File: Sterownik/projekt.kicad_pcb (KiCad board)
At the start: 2 copper layers, 59.7 x 52.1 mm, 73 parts, among them P3 CONN_01X05, P4 CONN_01X02, P5 CONN_01X02, P6 USB_OTG, P7 CONN_01X12, P8 CONN_01X02, SW1 SW_PUSH_SMALL, T1 Si2323DS, T10 Si2323DS, T12 2N7002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

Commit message: Additional changes
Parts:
- moved R14 7.85 mm to (193.5, 105.5), turned to 270 degrees
- moved R13 2.93 mm to (191.8, 105.5), turned to 90 degrees
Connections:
- C20 pad 1: VUSB_BUS -> VBUS
- C39 pad 1: VUSB_BUS -> VBUS
- C40 pad 1: VUSB_BUS -> VBUS
- C41 pad 1: VUSB_BUS -> VBUS
- R5 pad 1: VUSB_BUS -> VBUS
- T1 pad S: VUSB_BUS -> VBUS
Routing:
- net ON_BUT: track 7.24 -> 98.0 mm, vias 0 -> 1
- net CHARGE_SIGNAL: track 11.8 -> 51.0 mm, vias 0 -> 2
- net VUSB_BUS: track 14.7 -> 48.0 mm
- net MAIN_VOL: track 23.3 -> 44.2 mm, vias 2 -> 3
- net VON: track 20.0 -> 38.6 mm
- net CHARGE_ENABLE: track 20.0 -> 32.2 mm, vias 2 -> 4
- net TERMINATE: track 7.56 -> 15.1 mm
- net VBAT_ADC: track 18.2 -> 23.1 mm
- net VBUS: track 39.1 -> 42.5 mm
- net VBATTERY: track 19.8 -> 18.3 mm
- net MAINTAIN: track 45.2 -> 46.6 mm
- net Net-(R2-Pad1): track 12.8 -> 11.8 mm
- net GND: track 285.6 -> 286.3 mm
- net (no net): track 0.00 -> 0.51 mm

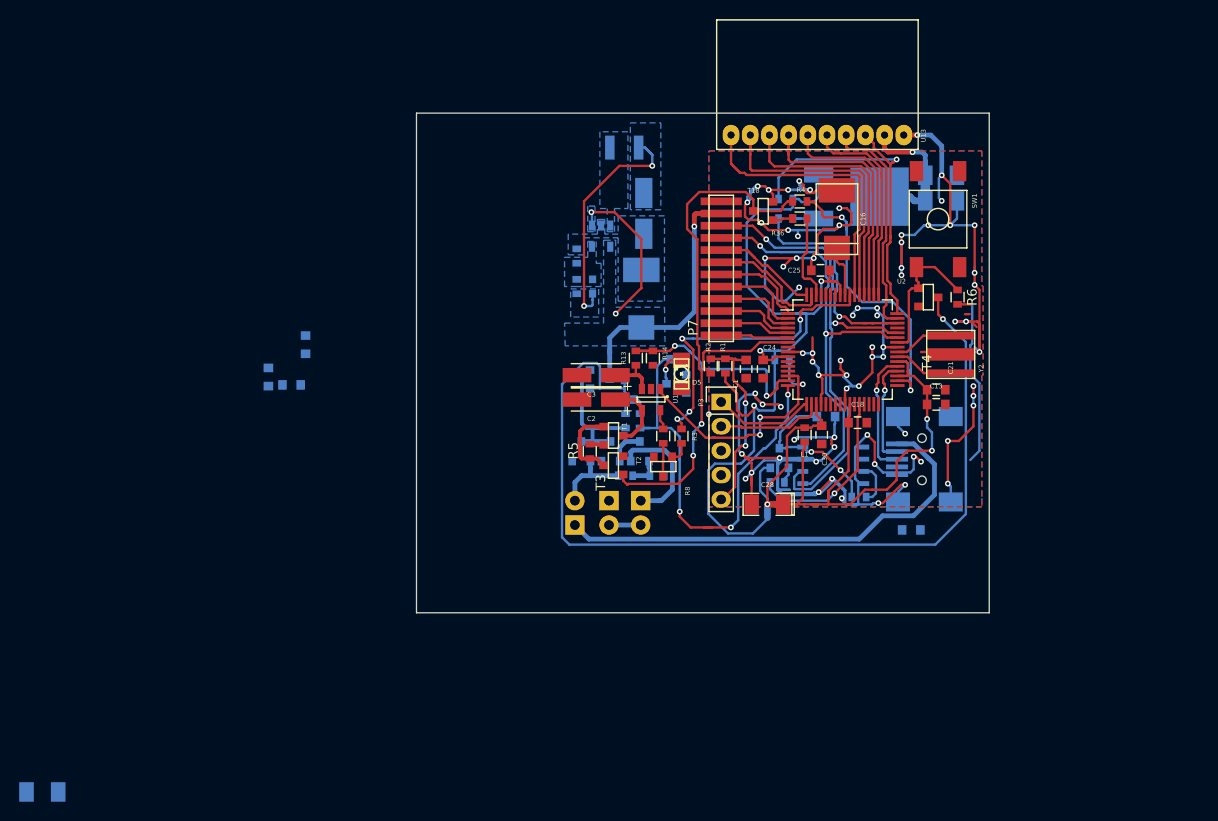
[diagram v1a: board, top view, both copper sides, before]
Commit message: 100% driver PCB routed - waiting for fixes
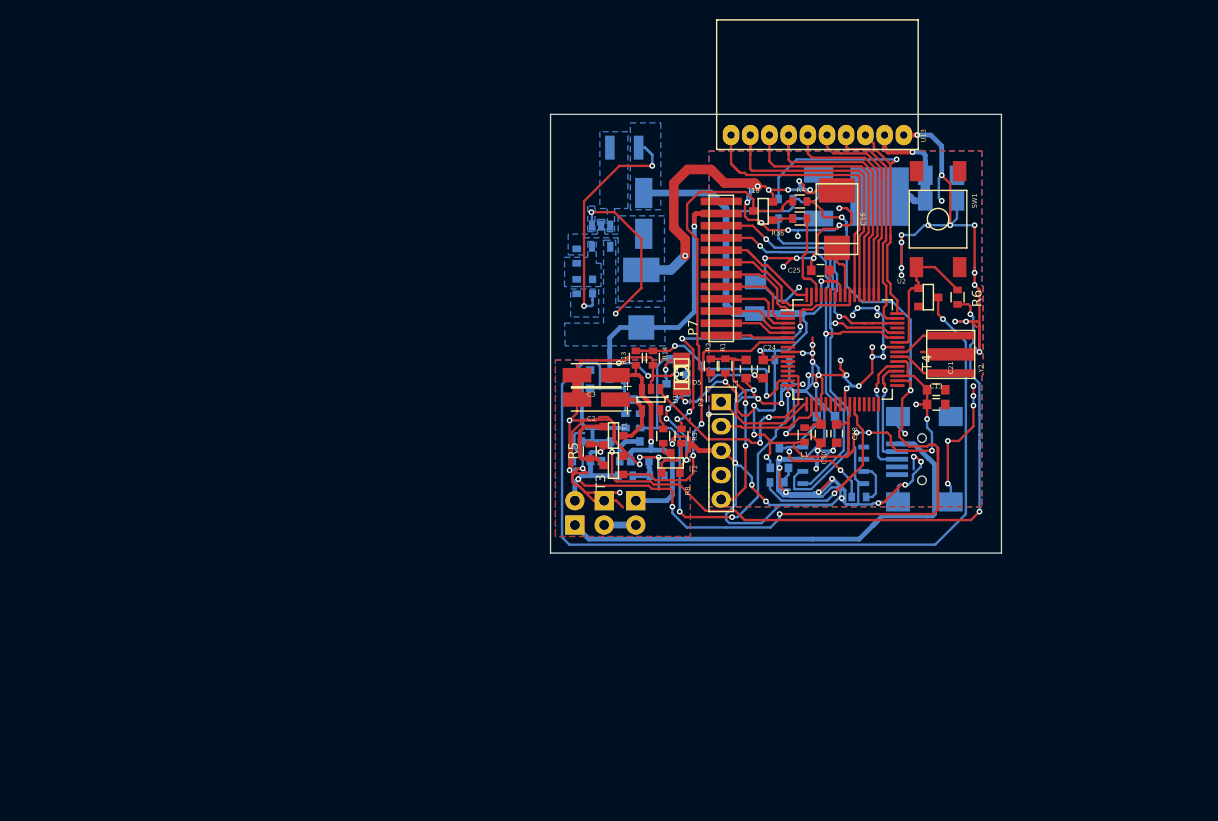
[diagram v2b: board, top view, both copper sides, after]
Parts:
- removed C20, C39, C40, C41: 100N, Capacitors_SMD:C_0603_HandSoldering
- removed C23: 100U, SMD_Packages:SMD-1206_Pol
- C28: moved to B.Cu
- moved C28 21.6 mm to (204.2, 99.3), turned to 90 degrees
- moved C18 2.47 mm to (212.7, 113.4), turned to 270 degrees
- moved T2 0.86 mm to (195.4, 116.5), turned to 0 degrees
- moved P4 0.51 mm to (188.5, 120.4)
- moved P8 0.51 mm to (191.8, 120.4)
- moved C30 0.14 mm to (211.1, 113.4)
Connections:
- C30 pad 1: VDD -> AVDD
- L1 pad 2: VDD -> AVDD
- U2 pad 19: VDD -> AVDD
- U2 pad 27: (no net) -> MEM_ENABLE
- U2 pad 28: MEM_ENABLE -> (no net)
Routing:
- net GND: track 286.3 -> 516.0 mm, vias 73 -> 92
- net VBUS: track 42.5 -> 110.6 mm, vias 2 -> 6
- net VON: track 38.6 -> 88.6 mm, vias 0 -> 3
- net VDD: track 187.5 -> 165.8 mm, vias 8 -> 14
- net VBATTERY: track 18.3 -> 26.0 mm, vias 0 -> 1
- net AVDD: track 0.00 -> 4.30 mm
- net CHARGE_STAT: track 28.3 -> 31.8 mm
- net MEM_ENABLE: track 18.6 -> 22.0 mm
- net Net-(R3-Pad1): track 2.24 -> 4.70 mm
- net MAINTAIN: track 46.6 -> 44.2 mm
- net VUSB_BUS: track 48.0 -> 49.9 mm
- net Net-(C35-Pad2): track 18.7 -> 16.9 mm
- net Net-(R8-Pad2): track 3.46 -> 1.72 mm
- net CHARGE_SIGNAL: track 51.0 -> 50.5 mm
- net (no net): track 0.51 -> 0.00 mm
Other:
- board size 59.7 x 52.1 mm -> 47 x 45.7 mm

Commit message: Fixes commit.
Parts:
- D5: moved to B.Cu
- moved T12 30.1 mm to (224.1, 97.4), turned to 90 degrees
- moved D5 29.8 mm to (223.4, 94.1), turned to 180 degrees
- moved R19 26.6 mm to (221.3, 97.4), turned to 90 degrees
- moved C28 2.86 mm to (207.0, 99.2)
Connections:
- R19 pad 2: MAINTAIN -> POWER_LED
- U2 pad 45: (no net) -> POWER_LED
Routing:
- net GND: track 516.0 -> 690.8 mm, vias 92 -> 125
- net MAIN_VOL: track 44.2 -> 54.7 mm
- net MAINTAIN: track 44.2 -> 36.1 mm
- net POWER_LED: track 0.00 -> 7.77 mm, vias 0 -> 1
- net VDD: track 165.8 -> 172.2 mm
- net VUSB_BUS: track 49.9 -> 56.0 mm
- net CLOCK_ENABLE: track 13.1 -> 10.8 mm
- net VBAT_ADC: track 23.1 -> 25.0 mm
- net WPWM1: track 30.8 -> 29.3 mm
- net TERMINATE: track 15.1 -> 16.6 mm
- net CHARGE_SIGNAL: track 50.5 -> 49.7 mm, vias 2 -> 4
- net WPWM2: track 28.6 -> 27.8 mm
- net VBUS: track 110.6 -> 111.2 mm
- net SCL: track 51.9 -> 51.3 mm
- net Net-(D5-Pad1): track 3.84 -> 3.43 mm, vias 1 -> 0

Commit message: Deleting additional files.
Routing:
- net VDD: track 172.2 -> 188.7 mm, vias 14 -> 15
- net GND: track 690.8 -> 688.5 mm, vias 125 -> 127
- net VBUS: track 111.2 -> 110.5 mm

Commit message: More fixes
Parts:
- added REF**: 1pin, Connect:1pin, F.Cu at (180.3, 83.9)
- added REF**: 1pin, Connect:1pin, F.Cu at (180.3, 89.0)
- added REF**: 1pin, Connect:1pin, F.Cu at (180.3, 120.8)
- added REF**: 1pin, Connect:1pin, F.Cu at (180.3, 115.7)
- added REF**: 1pin, Connect:1pin, F.Cu at (231.1, 120.8)
- added REF**: 1pin, Connect:1pin, F.Cu at (231.1, 115.7)
- added REF**: 1pin, Connect:1pin, F.Cu at (231.1, 97.9)
- added REF**: 1pin, Connect:1pin, F.Cu at (231.1, 103.0)
- added REF**: 2N7002-SOT23, Footprinty:2N7002-SOT23, F.Cu at (238.9, 90.3)
- C4: footprint Capacitors_Tantalum_SMD:TantalC_SizeX_EIA-7343 -> Footprinty:TantalC_SizeA_EIA-3216_HandSoldering
- moved C4 0.80 mm to (192.4, 98.6), turned to 90 degrees
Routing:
- net GND: track 688.5 -> 703.0 mm, vias 127 -> 134
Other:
- board size 47 x 45.7 mm -> 55.9 x 45.7 mm

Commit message: Working on sensor board
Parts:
- removed the REF** at (238.9, 90.3)
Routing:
- net GND: track 703.0 -> 751.5 mm, vias 134 -> 137
- net MAIN_VOL: track 54.5 -> 56.4 mm
- net VBUS: track 110.5 -> 111.1 mm
- net VDD: track 188.7 -> 188.2 mm

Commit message: Simplifiying all
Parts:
- moved REF** 2.54 mm to (180.3, 123.3)
- moved REF** 2.54 mm to (180.3, 118.2)
- moved REF** 2.54 mm to (231.1, 123.3)
- moved REF** 2.54 mm to (231.1, 118.2)
- moved REF** 1.27 mm to (180.3, 82.7)
- moved REF** 1.27 mm to (180.3, 87.8)
- moved P7 0.18 mm to (200.7, 103.0)
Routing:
- net CLOCK_ENABLE: track 10.8 -> 17.1 mm
- net GND: track 751.5 -> 747.4 mm, vias 137 -> 136
- net SCL: track 51.3 -> 54.0 mm
- net SDA: track 46.3 -> 47.6 mm
- net SOUND_ENABLE: track 8.26 -> 7.13 mm
- net CLOCK: track 9.23 -> 8.34 mm
- net CONV_ENABLE: track 8.58 -> 7.72 mm
- net SUSPEND: track 10.7 -> 9.91 mm
- net HUM_ENABLE: track 11.3 -> 10.5 mm
- net ADCDATA: track 10.1 -> 9.38 mm

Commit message: Simplier version - first fixes
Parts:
- removed P7: CONN_01X12, Footprinty:DS1065-02-1-12S8BS
- removed R32, R35, R5: 100K, Resistors_SMD:R_0603
- removed REF** (x8): 1pin, Connect:1pin
- removed T1: Si2323DS, Footprinty:SOT23
- removed T15, T3: 2N7002, Footprinty:2N7002-SOT23
- removed T17: NTD25P03L, SMD_Packages:DPAK-3_GDS
- added P1: CONN_01X08, Footprinty:DS1065-02-1X8S8BS, F.Cu at (200.7, 103.0)
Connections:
- net VON renamed VINPUT
- C2 pad 1: Net-(C2-Pad1) -> VBUS
- C35 pad 2: Net-(C35-Pad2) -> VDD
- C36 pad 1: Net-(C36-Pad1) -> VDD
- C42 pad 1: Net-(C36-Pad1) -> VDD
- R34 pad 1: Net-(C35-Pad2) -> VDD
- U1 pad 4: Net-(C2-Pad1) -> VBUS
- U11 pad 8: Net-(C35-Pad2) -> VDD
- U13 pad 2: Net-(C36-Pad1) -> VDD
- U2 pad 1: HUM_ENABLE -> (no net)
- U2 pad 27: MEM_ENABLE -> (no net)
- U2 pad 46: COMM_ENABLE -> (no net)
- U2 pad 5: CONV_ENABLE -> (no net)
- U2 pad 6: SOUND_ENABLE -> (no net)
- U2 pad 63: PRESS_ENABLE -> (no net)
- U2 pad 64: CLOCK_ENABLE -> (no net)
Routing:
- net CHARGE_SIGNAL: track 49.7 -> 4.99 mm, vias 4 -> 0
- net VDD: track 188.2 -> 211.6 mm
- net COMM_ENABLE: track 22.8 -> 0.00 mm, vias 1 -> 0
- net MEM_ENABLE: track 22.0 -> 0.00 mm, vias 1 -> 0
- net CLOCK_ENABLE: track 17.1 -> 0.00 mm
- net Net-(C35-Pad2): track 16.9 -> 0.00 mm, vias 2 -> 0
- net Net-(C36-Pad1): track 16.0 -> 0.00 mm, vias 1 -> 0
- net PRESS_ENABLE: track 15.7 -> 0.00 mm
- net HUM_ENABLE: track 10.5 -> 0.00 mm
- net Net-(R5-Pad2): track 9.02 -> 0.00 mm
- net CONV_ENABLE: track 7.72 -> 0.00 mm
- net Net-(C2-Pad1): track 7.35 -> 0.00 mm
- net SOUND_ENABLE: track 7.13 -> 0.00 mm
- net MAIN_VOL: track 56.5 -> 62.5 mm
- net Net-(R35-Pad1): track 3.20 -> 0.00 mm
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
